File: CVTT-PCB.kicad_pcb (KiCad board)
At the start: 4 copper layers, 66 x 88 mm, 58 parts, among them J1 SERVO1, J2 SERVO2, J3 LCD SCREEN, J4 LCD BUTTONS, J5 Conn_ARM_SWD_TagConnect_TC2030, J6 USB_B_Micro, P2 DC2, P5 DC1, P8 STEPPER, Q7 BSS138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

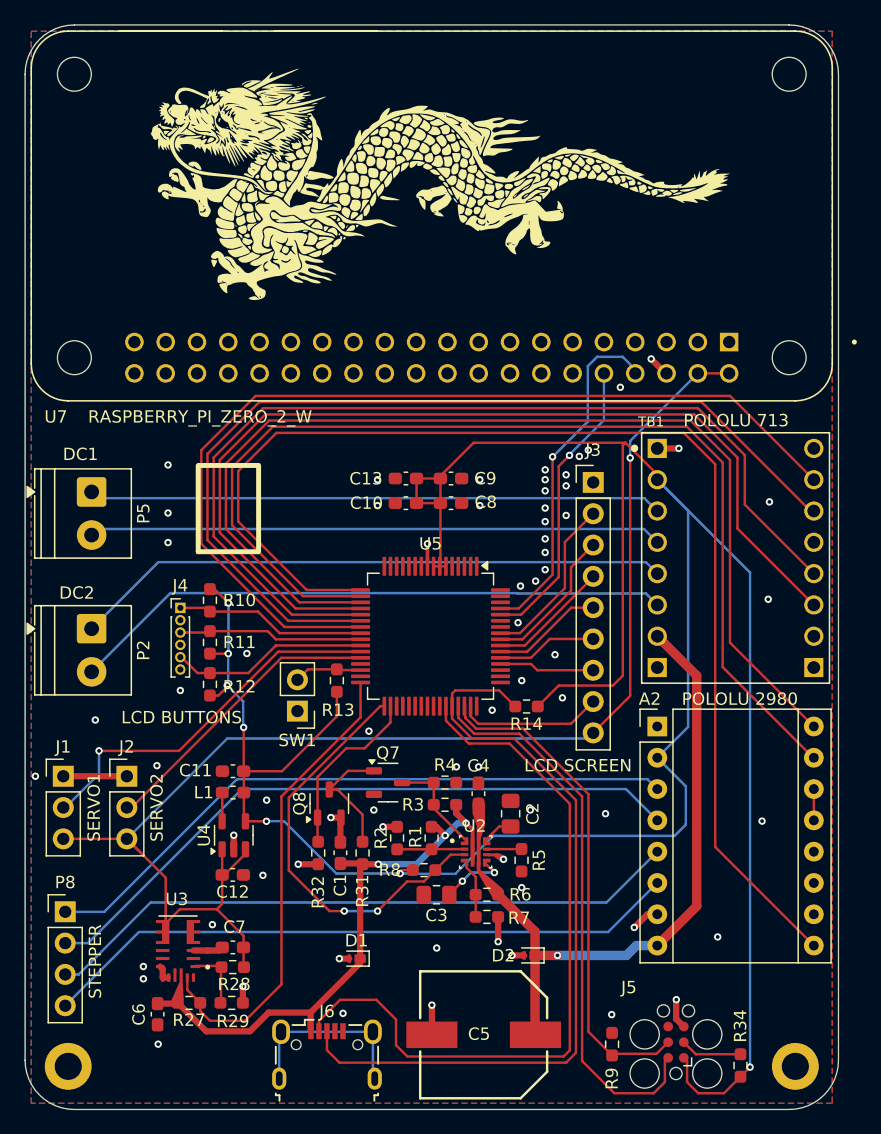
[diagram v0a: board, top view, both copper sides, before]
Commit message: Add LED indicators
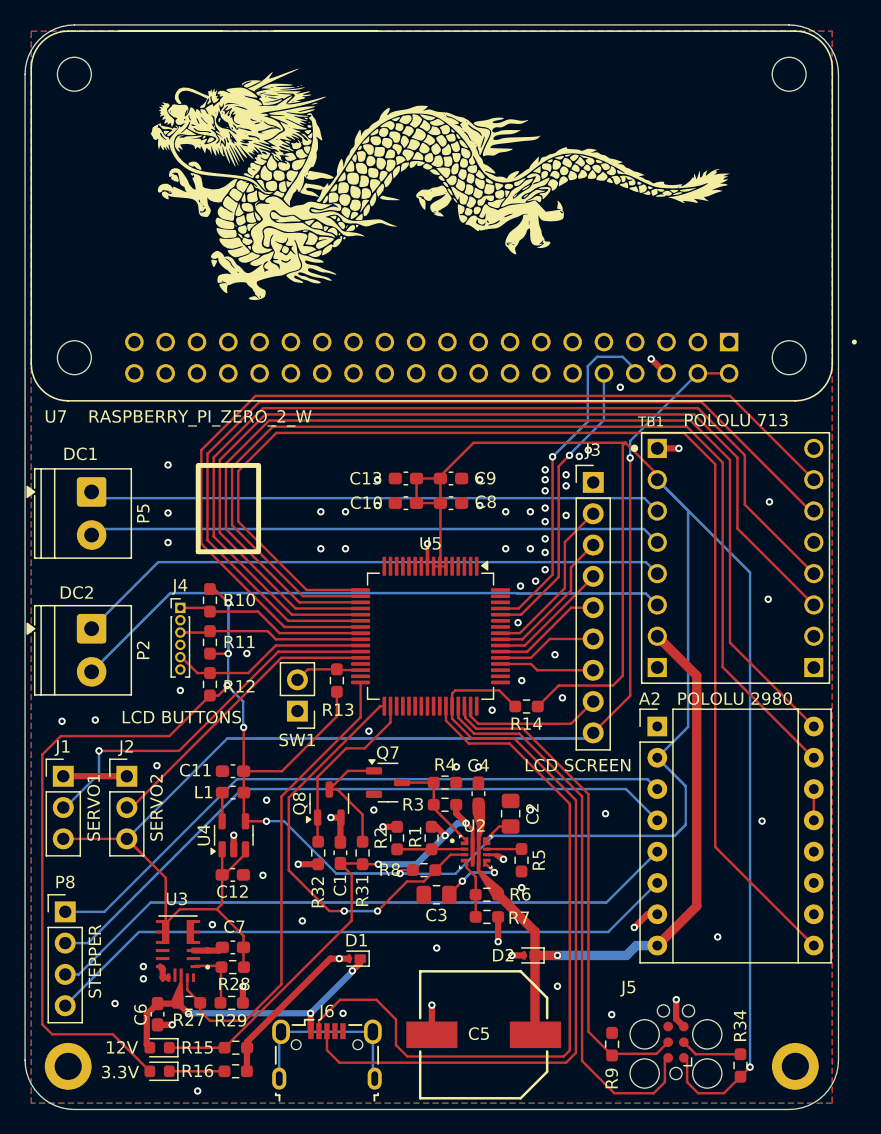
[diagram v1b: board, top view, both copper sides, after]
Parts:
- added D3: 12V, LED_SMD:LED_0603_1608Metric, F.Cu at (116.9, 135.5)
- added D4: 3.3V, LED_SMD:LED_0603_1608Metric, F.Cu at (116.9, 137.4)
- added R15: 1k, Resistor_SMD:R_0603_1608Metric_Pad0.98x0.95mm_HandSolder, F.Cu at (123.1, 135.5)
- added R16: 1k, Resistor_SMD:R_0603_1608Metric_Pad0.98x0.95mm_HandSolder, F.Cu at (123.1, 137.4)
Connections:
- C1 pad 1: +12V -> Net-(D3-K)
- R1 pad 1: +12V -> Net-(D3-K)
- R3 pad 1: +12V -> Net-(D3-K)
- R31 pad 1: +12V -> Net-(D3-K)
- U2 pad 5: +12V -> Net-(D3-K)
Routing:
- net +3.3V: track 227.1 -> 274.9 mm
- net Net-(D3-K): track 0.00 -> 39.2 mm, vias 0 -> 3
- net +12V: track 44.2 -> 24.5 mm
- net GND: track 31.4 -> 45.3 mm, vias 68 -> 80
- net Net-(D4-K): track 0.00 -> 4.47 mm

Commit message: Update schem and layout
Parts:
- added D5: PG, LED_SMD:LED_0603_1608Metric, F.Cu at (136.4, 126.6)
- added R17: 53.6k, Resistor_SMD:R_0603_1608Metric_Pad0.98x0.95mm_HandSolder, F.Cu at (125.5, 128.0)
- added R18: 10k, Resistor_SMD:R_0603_1608Metric_Pad0.98x0.95mm_HandSolder, F.Cu at (153.5, 116.5)
- added R19: 10k, Resistor_SMD:R_0603_1608Metric_Pad0.98x0.95mm_HandSolder, F.Cu at (134.1, 93.6)
- J4: footprint Connector_PinHeader_1.00mm:PinHeader_1x06_P1.00mm_Vertical -> Connector_PinHeader_2.54mm:PinHeader_1x06_P2.54mm_Vertical
- L1: footprint Inductor_SMD:L_0603_1608Metric_Pad1.05x0.95mm_HandSolder -> Inductor_SMD:L_Bourns_SRU5016_5.2x5.2mm
- R8: value 47k -> 3.3k
- moved J4 5.12 mm to (117.8, 94.7)
- moved C11 5.06 mm to (124.6, 108.3), turned to 0 degrees
- moved L1 2.46 mm to (124.0, 112.6), turned to 90 degrees
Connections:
- A2 pad 13: Net-(A2-~{RESET}) -> /DRV_RST
- A2 pad 14: Net-(A2-~{RESET}) -> /DRV_SLEEP
- R27 pad 2: /BUCK_EN -> Net-(U3-EN)
- TB1 pad 10: unconnected-(TB1-PWMB-Pad10) -> /PMWB
- TB1 pad 13: unconnected-(TB1-~{STBY}-Pad13) -> /STBY
- TB1 pad 16: unconnected-(TB1-PWMA-Pad16) -> /PMWA
- U3 pad 17: /BUCK_EN -> Net-(U3-EN)
- U3 pad 18: unconnected-(U3-AAM-Pad18) -> Net-(U3-AAM)
- U5 pad 32: /BUCK_EN -> unconnected-(U5-PB12-Pad32)
- U5 pad 40: unconnected-(U5-PD8-Pad40) -> /DRV_SLEEP
- U5 pad 41: unconnected-(U5-PD9-Pad41) -> /DRV_RST
- U5 pad 48: unconnected-(U5-PC8-Pad48) -> /STBY
- U5 pad 51: unconnected-(U5-PD1-Pad51) -> /PMWB
- U5 pad 58: unconnected-(U5-PB4-Pad58) -> /PMWA
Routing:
- net /STBY: track 0.00 -> 56.5 mm, vias 0 -> 1
- net /BUCK_EN: track 38.4 -> 0.00 mm
- net /DRV_SLEEP: track 0.00 -> 36.8 mm, vias 0 -> 1
- net /DRV_RST: track 0.00 -> 36.5 mm, vias 0 -> 1
- net /PMWA: track 0.00 -> 35.0 mm, vias 0 -> 1
- net /PMWB: track 0.00 -> 28.7 mm, vias 0 -> 1
- net +3.3V: track 274.9 -> 255.1 mm, vias 7 -> 9
- net Net-(U3-AAM): track 0.00 -> 6.81 mm, vias 0 -> 2
- net GND: track 45.3 -> 51.6 mm, vias 80 -> 88
- net /DRV_EN: track 99.7 -> 105.9 mm
- net /LCD_BUTTONU: track 15.5 -> 19.8 mm
- net /PG: track 34.2 -> 36.9 mm
- net Net-(A2-~{RESET}): track 2.54 -> 0.00 mm
- net Net-(U3-EN): track 0.00 -> 2.13 mm
- net +5V: track 111.0 -> 109.2 mm, vias 1 -> 3
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
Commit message: Update pinout
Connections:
- U5 pad 1: unconnected-(U5-PC11-Pad1) -> /PMWA
- U5 pad 39: unconnected-(U5-PC7-Pad39) -> /PMWB
- U5 pad 51: /PMWB -> unconnected-(U5-PD1-Pad51)
- U5 pad 58: /PMWA -> unconnected-(U5-PB4-Pad58)
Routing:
- net /PMWB: track 28.7 -> 37.2 mm
- net Net-(P2-B1): track 49.2 -> 50.4 mm
- net /DRV_RST: track 36.5 -> 37.1 mm
- net GND: vias 88 -> 89

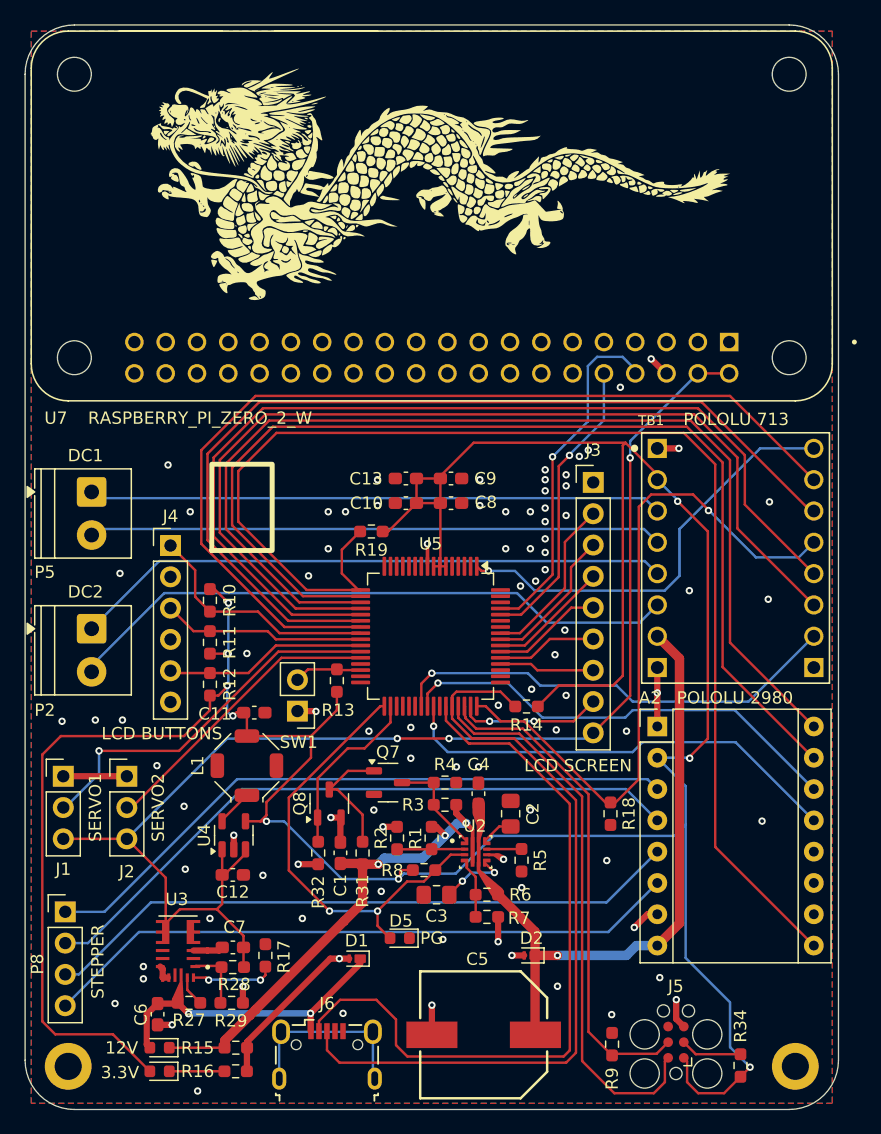
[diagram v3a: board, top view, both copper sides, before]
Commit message: add RGB led status indicator
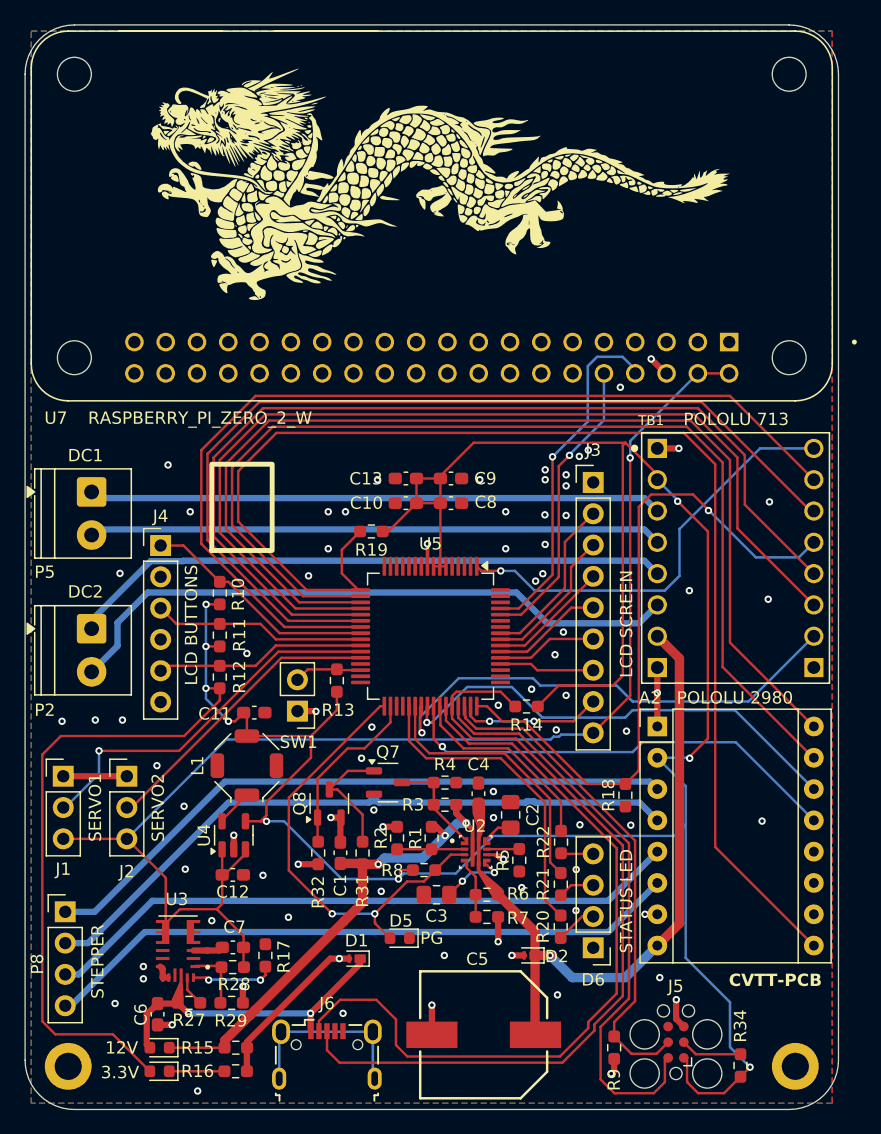
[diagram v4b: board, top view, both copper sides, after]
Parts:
- added D6: STATUS LED, Connector_PinHeader_2.54mm:PinHeader_1x04_P2.54mm_Vertical, F.Cu at (152.1, 127.4)
- added R20: 160, Resistor_SMD:R_0603_1608Metric_Pad0.98x0.95mm_HandSolder, F.Cu at (149.5, 125.7)
- added R21: 100, Resistor_SMD:R_0603_1608Metric_Pad0.98x0.95mm_HandSolder, F.Cu at (149.5, 122.2)
- added R22: 100, Resistor_SMD:R_0603_1608Metric_Pad0.98x0.95mm_HandSolder, F.Cu at (149.5, 118.8)
- moved R18 1.93 mm to (154.7, 115.0)
- moved R10 0.99 mm to (121.8, 98.6), turned to 90 degrees
- moved R12 0.99 mm to (121.8, 105.4)
- moved R11 0.99 mm to (121.8, 102.0)
- moved J4 0.80 mm to (117.0, 94.7)
- moved R9 0.33 mm to (153.8, 135.5), turned to -90 degrees
- moved R5 0.19 mm to (146.1, 120.3)
- moved C2 0.10 mm to (145.4, 116.6)
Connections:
- U5 pad 37: unconnected-(U5-PA9/UCPD1_DBCC1-Pad37) -> /LED_R
- U5 pad 38: unconnected-(U5-PC6-Pad38) -> /LED_G
- U5 pad 42: unconnected-(U5-PA10/UCPD1_DBCC2-Pad42) -> /LED_B
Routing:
- net /LED_R: track 0.00 -> 25.6 mm
- net /LED_G: track 0.00 -> 22.0 mm
- net /LED_B: track 0.00 -> 16.3 mm
- net Net-(D6-RA): track 0.00 -> 3.36 mm
- net /PA11_USB_D-: track 59.2 -> 62.3 mm
- net /PA12_USB_D+: track 63.4 -> 66.5 mm
- net Net-(D6-GA): track 0.00 -> 2.97 mm
- net /PMWB: track 37.2 -> 39.8 mm
- net Net-(D6-BA): track 0.00 -> 2.63 mm
- net /PA13_SWDIO: track 45.4 -> 47.3 mm
- net /STBY: track 56.5 -> 54.9 mm
- net Net-(P2-B1): track 50.4 -> 51.9 mm
- net /+12V MOTOR: track 51.0 -> 52.5 mm
- net /DRV_SLEEP: track 36.8 -> 37.9 mm
- net Net-(A2-1A): track 54.3 -> 53.5 mm
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
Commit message: update layout
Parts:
- U7: value RASPBERRY_PI_ZERO_2_W -> RASPBERRY PI ZERO 2 W
